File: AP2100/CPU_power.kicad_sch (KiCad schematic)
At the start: 70 parts, among them IC3 AS4C256M16D4-75BCN, IC4 AS4C256M16D4-75BCN, U1 LS1043ASE7KQB

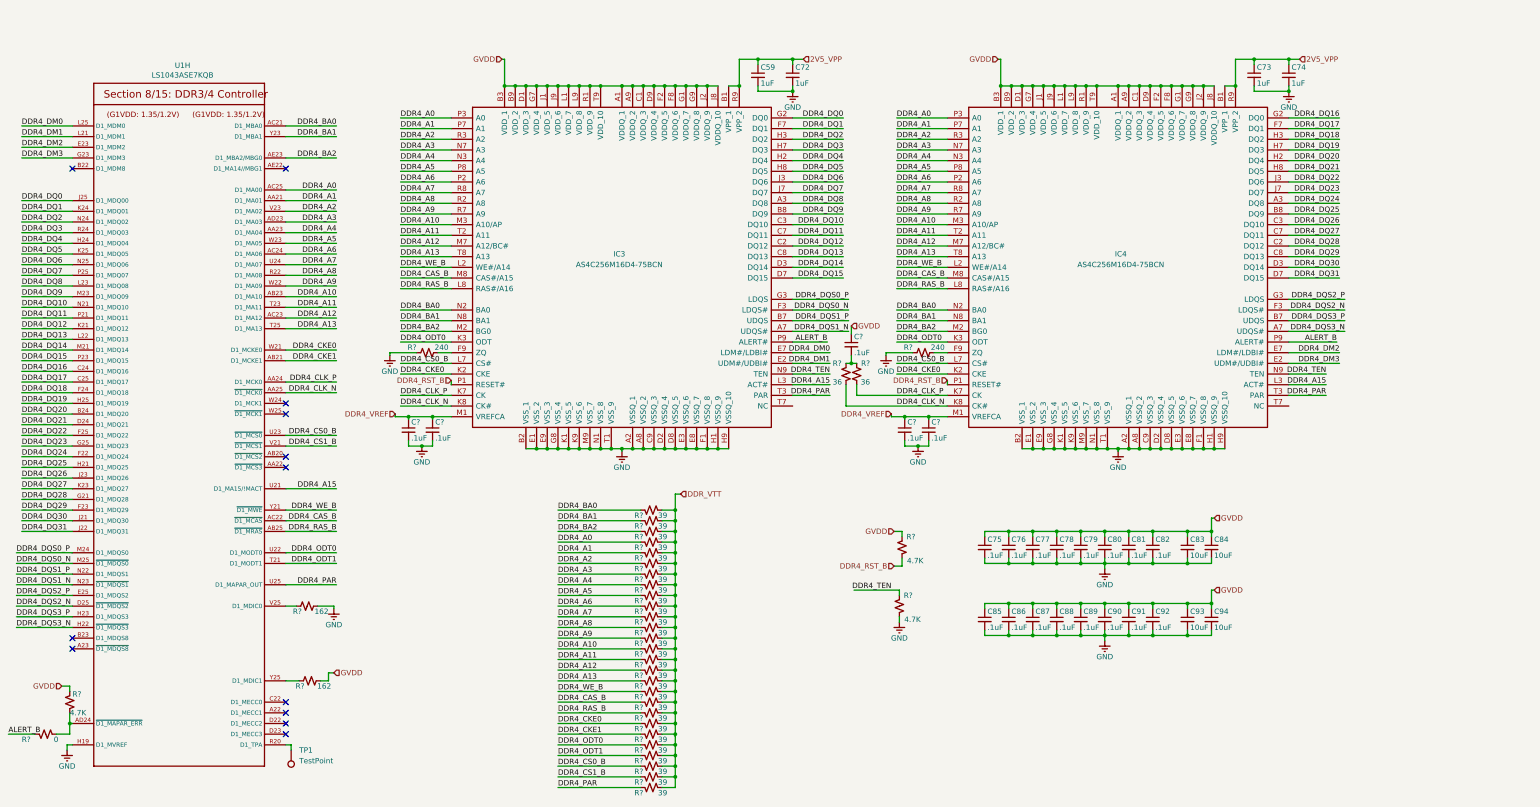
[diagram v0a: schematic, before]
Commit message: Add CPU Power block. Change global labels to hierarchical and link them at top page Add 5V USB power supply
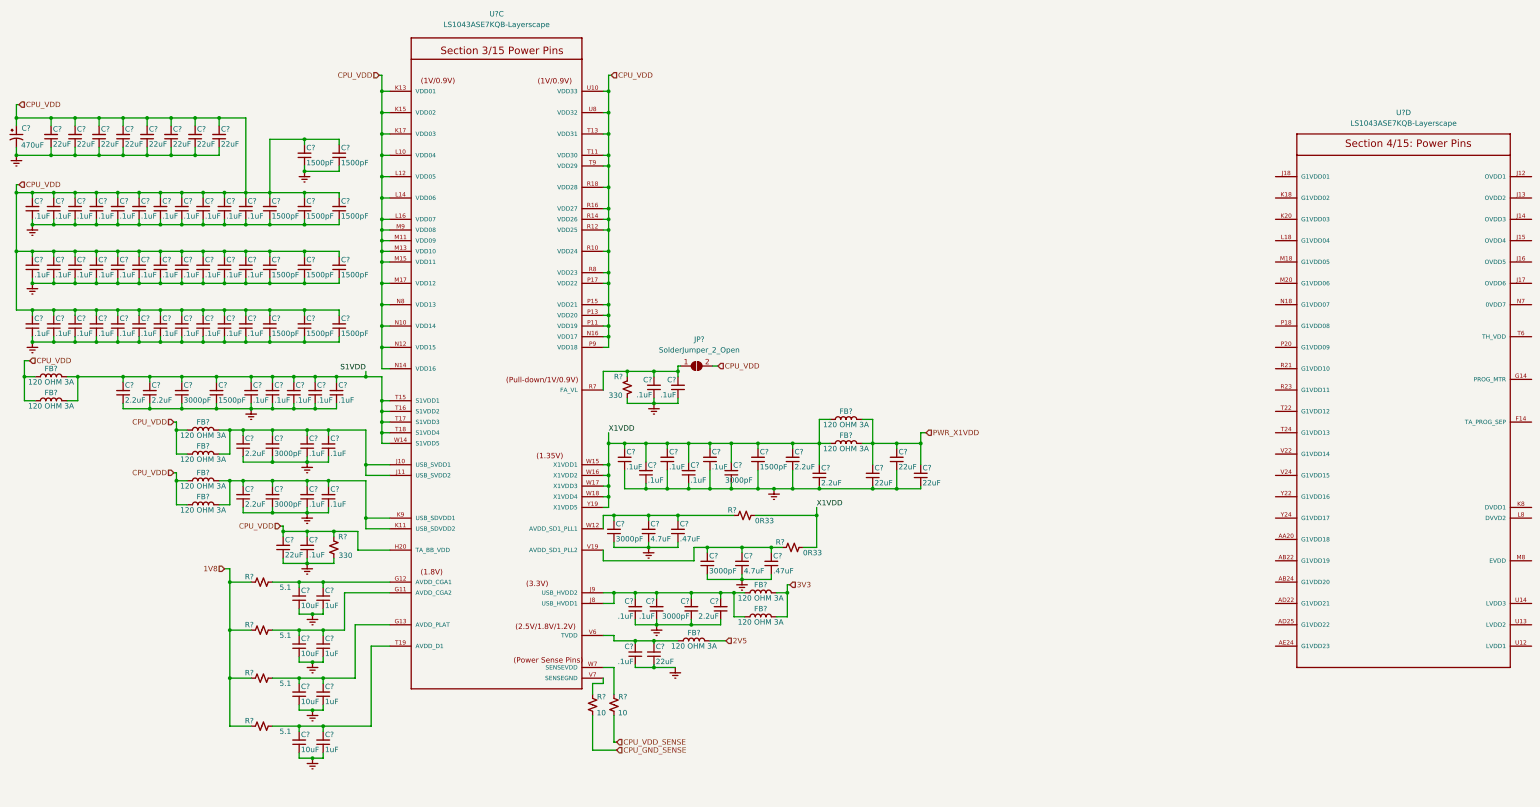
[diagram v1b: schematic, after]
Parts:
- removed C59, C72, C73, C74: 1uF, Capacitor_SMD:C_0402_1005Metric, symbol Device:C_Small
- removed C75, C76, C77, C78, C79, C80, C81, C82, C85, C86, C87, C88, C89, C90, C91, C92, C? (x5): .1uF, Capacitor_SMD:C_0402_1005Metric, symbol Device:C_Small
- removed C83, C84, C93, C94: 10uF, Capacitor_SMD:C_0805_2012Metric, symbol Device:C_Small
- removed IC3, IC4: AS4C256M16D4-75BCN, Scott:BGA96C80P9X16_750X1350X120, symbol Scott:AS4C256M16D4
- removed R? (x27): 39, Resistor_SMD:R_0402_1005Metric, symbol Device:R_Small_US
- removed R? (x2): 36, Resistor_SMD:R_0402_1005Metric, symbol Device:R_Small_US
- removed R? (x2): 240, Resistor_SMD:R_0402_1005Metric, symbol Device:R_Small_US
- removed R? (x3): 4.7K, Resistor_SMD:R_0402_1005Metric, symbol Device:R_Small_US
- removed R?: 0, Resistor_SMD:R_0402_1005Metric, symbol Device:R_Small_US
- removed R? (x2): 162, Resistor_SMD:R_0402_1005Metric, symbol Device:R_Small_US
- removed TP1: TestPoint, symbol Connector:TestPoint
- removed U1: LS1043ASE7KQB, PLS1043ASE7QQA:BGA621C80P25X25_2100X2100X192N, symbol AP2100-rescue:LS1043ASE7KQB-Layerscape
- added C? (x53): .1uF, Capacitor_SMD:C_0201_0603Metric, symbol Device:C_Small
- added C? (x7): 2.2uF, Capacitor_SMD:C_0402_1005Metric, symbol Device:C_Small
- added C? (x13): 22uF, Capacitor_SMD:C_0805_2012Metric, symbol Device:C_Small
- added C? (x2): 4.7uF, Capacitor_SMD:C_0805_2012Metric, symbol Device:C_Small
- added C? (x7): 3000pF, Capacitor_SMD:C_0402_1005Metric, symbol Device:C_Small
- added C? (x12): 1500pF, Capacitor_SMD:C_0201_0603Metric, symbol Device:C_Small
- added C? (x4): 1uF, Capacitor_SMD:C_0201_0603Metric, symbol Device:C_Small
- added C? (x4): 10uF, Capacitor_SMD:C_0805_2012Metric, symbol Device:C_Small
- added C?: 470uF, Capacitor_SMD:C_Elec_10x10.2, symbol Device:CP1_Small
- added C?: 1500pF, Capacitor_SMD:C_0402_1005Metric, symbol Device:C_Small
- added C? (x2): .47uF, Capacitor_SMD:C_0603_1608Metric, symbol Device:C_Small
- added FB? (x11): 120 OHM 3A, Inductor_SMD:L_0603_1608Metric, symbol Device:L
- added JP?: SolderJumper_2_Open, symbol Jumper:SolderJumper_2_Open
- added R? (x2): 10, Resistor_SMD:R_0402_1005Metric, symbol Device:R_Small_US
- added R? (x4): 5.1, Resistor_SMD:R_0402_1005Metric, symbol Device:R_Small_US
- added R? (x2): 330, Resistor_SMD:R_0402_1005Metric, symbol Device:R_Small_US
- added R? (x2): 0R33, Resistor_SMD:R_0402_1005Metric, symbol Device:R_Small_US
- added U? (x2): LS1043ASE7KQB-Layerscape, PLS1043ASE7QQA:BGA621C80P25X25_2100X2100X192N, symbol AP2100-rescue:LS1043ASE7KQB-Layerscape
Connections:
- net GND: now also C?.1, C?.1, C?.1, C?.1, C?.1, C?.1, C?.1, C?.1, C?.1, C?.1, C?.1, C?.1, C?.1, C?.1, C?.1, C?.1, C?.1, C?.1, C?.1, C?.1, C?.1, C?.1, C?.1, C?.1, C?.1, C?.1, C?.1, C?.1, C?.1, C?.1, C?.1, C?.1, C?.1, C?.1, C?.1, C?.1, C?.1, C?.1, C?.1, C?.1, C?.1, C?.1, C?.1, C?.1, C?.1, C?.1, C?.1, C?.1, C?.1, C?.1, C?.1, C?.1, C?.1, C?.1, C?.1, C?.1, C?.1, C?.1, C?.1, C?.1, C?.1, C?.1, C?.1, C?.1, C?.1, C?.1, C?.1, C?.1, C?.1, C?.1, C?.1, C?.1, C?.1, C?.1, C?.1, C?.1, C?.1, C?.1, C?.1, C?.1, C?.1, C?.1, C?.1, C?.1, C?.1, C?.1, C?.1, C?.1, C?.1, C?.1, C?.1, C?.1, C?.1, C?.1, C?.1, C?.1, C?.1, C?.1, C?.1, C?.1, C?.1, C?.1, C?.1, C?.1, C?.1, C?.2, R?.1, R?.1
- new net: C?.2, C?.2, C?.2, R?.1, U?.W12 (AVDD_SD1_PLL1)
- new net: R?.2, U?.W7 (SENSEVDD)
- new net: C?.2, C?.2, R?.2, U?.G11 (AVDD_CGA2)
- new net: C?.2, C?.2, FB?.2, U?.V6 (TVDD)
- new net: C?.2, C?.2, R?.2, U?.G12 (AVDD_CGA1)
- new net: C?.2, C?.2, C?.2, C?.2, FB?.2, FB?.2, U?.K11 (USB_SDVDD2), U?.K9 (USB_SDVDD1)
- new net: C?.2, C?.2, C?.2, C?.2, FB?.2, FB?.2, U?.J8 (USB_HVDD1), U?.J9 (USB_HVDD2)
- new net: C?.2, C?.2, R?.2, U?.T19 (AVDD_D1)
- new net: C?.2, C?.2, C?.2, C?.2, FB?.2, FB?.2, U?.J10 (USB_SVDD1), U?.J11 (USB_SVDD2)
- new net: C?.2, C?.2, JP?.1 (A), R?.2, U?.R7 (FA_VL)
- new net: C?.2, C?.2, C?.2, R?.1, U?.V19 (AVDD_SD1_PLL2)
- new net: C?.2, C?.2, R?.2, U?.G13 (AVDD_PLAT)
- new net: R?.2, U?.V7 (SENSEGND)
- new net 1V8: R?.1, R?.1, R?.1, R?.1
- new net 2V5: FB?.1
- new net 3V3: FB?.1, FB?.1
- new net CPU_GND_SENSE: R?.1
- new net CPU_VDD: C?.1, C?.2, C?.2, C?.2, C?.2, C?.2, C?.2, C?.2, C?.2, C?.2, C?.2, C?.2, C?.2, C?.2, C?.2, C?.2, C?.2, C?.2, C?.2, C?.2, C?.2, C?.2, C?.2, C?.2, C?.2, C?.2, C?.2, C?.2, C?.2, C?.2, C?.2, C?.2, C?.2, C?.2, C?.2, C?.2, C?.2, C?.2, C?.2, C?.2, C?.2, C?.2, C?.2, C?.2, C?.2, C?.2, C?.2, C?.2, C?.2, C?.2, C?.2, C?.2, C?.2, C?.2, C?.2, FB?.1, FB?.1, FB?.1, FB?.1, FB?.1, FB?.1, JP?.2 (B), R?.2, U?.H20 (TA_BB_VDD), U?.K13 (VDD01), U?.K15 (VDD02), U?.K17 (VDD03), U?.L10 (VDD04), U?.L12 (VDD05), U?.L14 (VDD06), U?.L16 (VDD07), U?.M11 (VDD09), U?.M13 (VDD10), U?.M15 (VDD11), U?.M17 (VDD12), U?.M9 (VDD08), U?.N10 (VDD14), U?.N12 (VDD15), U?.N14 (VDD16), U?.N16 (VDD17), U?.N8 (VDD13), U?.P11 (VDD19), U?.P13 (VDD20), U?.P15 (VDD21), U?.P17 (VDD22), U?.P9 (VDD18), U?.R10 (VDD24), U?.R12 (VDD25), U?.R14 (VDD26), U?.R16 (VDD27), U?.R18 (VDD28), U?.R8 (VDD23), U?.T11 (VDD30), U?.T13 (VDD31), U?.T9 (VDD29), U?.U10 (VDD33), U?.U8 (VDD32)
- new net CPU_VDD_SENSE: R?.1
- new net PWR_X1VDD: C?.2, C?.2, C?.2, FB?.2, FB?.2
- new net S1VDD: C?.2, C?.2, C?.2, C?.2, C?.2, C?.2, C?.2, C?.2, C?.2, FB?.2, FB?.2, U?.T15 (S1VDD1), U?.T16 (S1VDD2), U?.T17 (S1VDD3), U?.T18 (S1VDD4), U?.W14 (S1VDD5)
- new net X1VDD: C?.2, C?.2, C?.2, C?.2, C?.2, C?.2, C?.2, C?.2, C?.2, FB?.1, FB?.1, R?.2, R?.2, U?.W15 (X1VDD1), U?.W16 (X1VDD2), U?.W17 (X1VDD3), U?.W18 (X1VDD4), U?.Y19 (X1VDD5)
- no-connect marks 12 -> 0
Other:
- company: IS ImageStream Internet Solutions, Inc. -> (none)
- title: AP2100 -> (none)

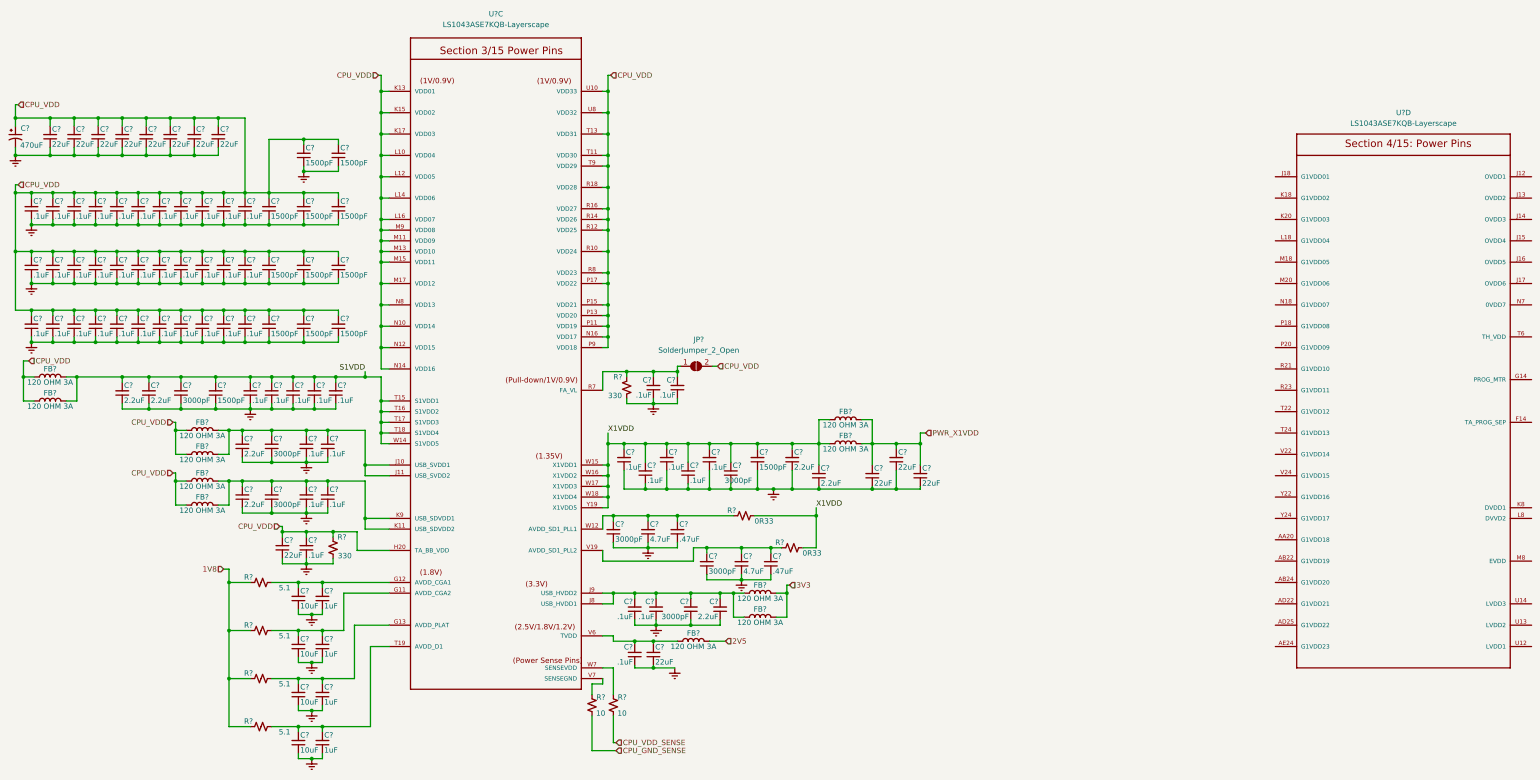
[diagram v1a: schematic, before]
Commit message: Add 2nd CPU power page. Start reset block
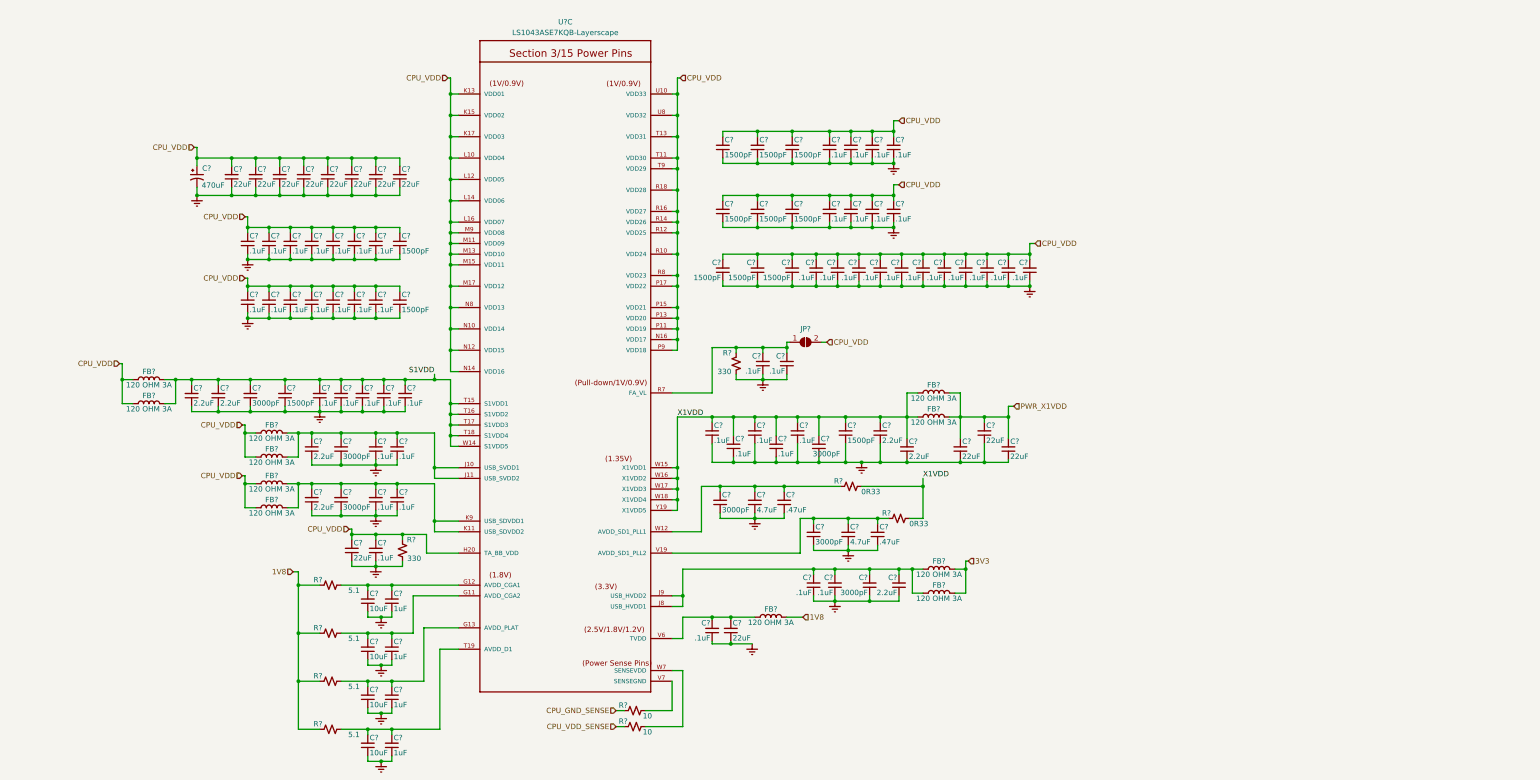
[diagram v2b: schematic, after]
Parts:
- removed R?: 10, Resistor_SMD:R_0402_1005Metric, symbol Device:R_Small_US
- removed U?: LS1043ASE7KQB-Layerscape, PLS1043ASE7QQA:BGA621C80P25X25_2100X2100X192N, symbol AP2100-rescue:LS1043ASE7KQB-Layerscape
- added R?: 10, Resistor_SMD:R_0402_1005Metric, symbol Device:R_Small_US
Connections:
- net 2V5 is gone; now on net 1V8: FB?.1
- net CPU_GND_SENSE: now also R?.2; no longer R?.1
- net CPU_VDD_SENSE: now also R?.2
- net at U?.W7 (SENSEVDD): now also R?.1
- net at U?.V7 (SENSEGND): now also R?.1; no longer R?.2
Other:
- moved on the sheet: C?, FB?, JP?, R?, U?C

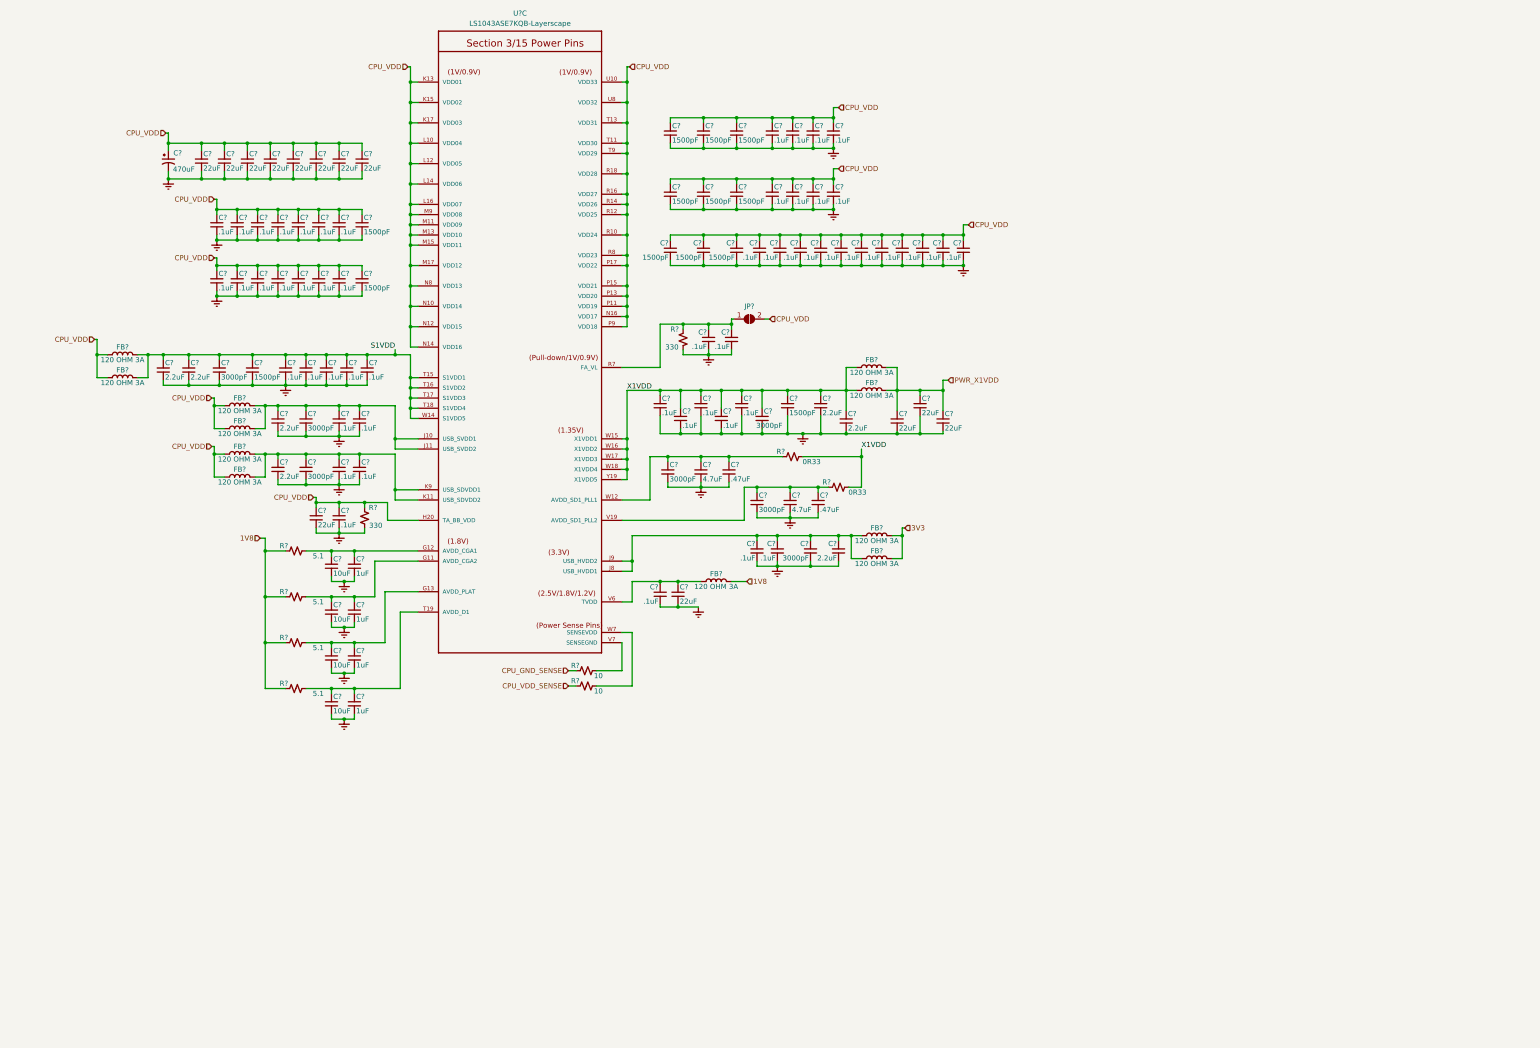
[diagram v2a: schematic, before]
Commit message: Add clocking and start of ethernet
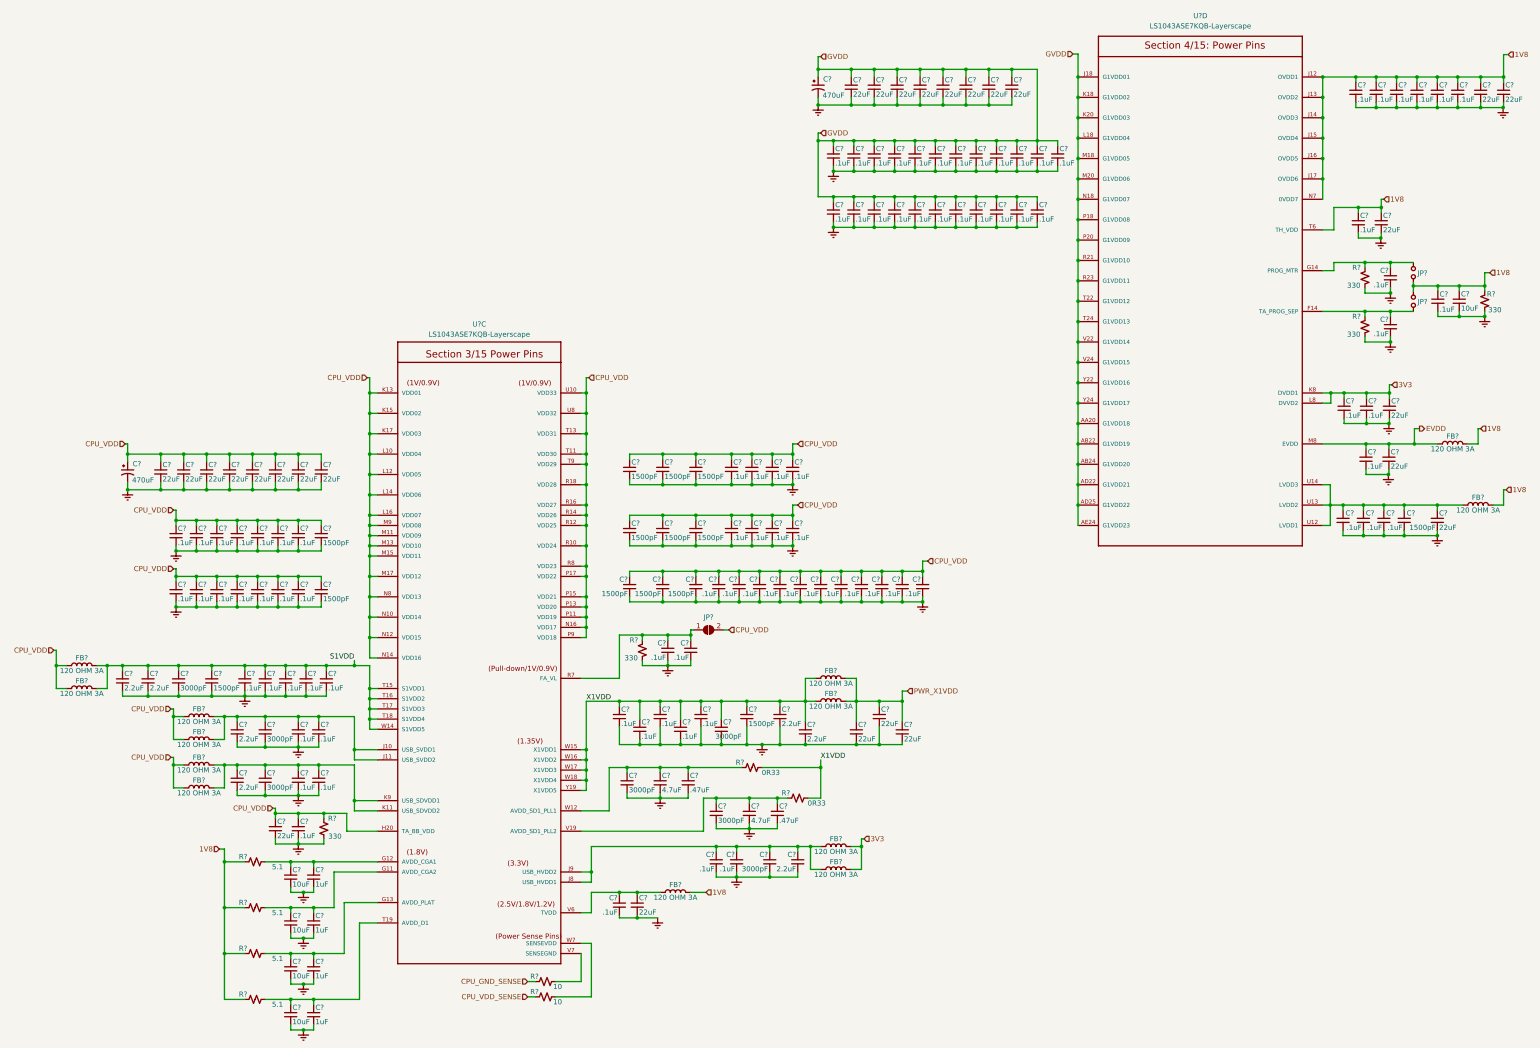
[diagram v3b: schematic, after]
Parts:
- added C? (x39): .1uF, Capacitor_SMD:C_0201_0603Metric, symbol Device:C_Small
- added C? (x14): 22uF, Capacitor_SMD:C_0805_2012Metric, symbol Device:C_Small
- added C?: 10uF, Capacitor_SMD:C_0805_2012Metric, symbol Device:C_Small
- added C?: 1500pF, Capacitor_SMD:C_0201_0603Metric, symbol Device:C_Small
- added C?: 470uF, Capacitor_SMD:C_Elec_10x10.2, symbol Device:CP1_Small
- added FB? (x2): 120 OHM 3A, Inductor_SMD:L_0603_1608Metric, symbol Device:L
- added JP? (x2): SolderJumper_2_Open, symbol Device:Jumper_NO_Small
- added R? (x3): 330, Resistor_SMD:R_0402_1005Metric, symbol Device:R_Small_US
- added U?: LS1043ASE7KQB-Layerscape, PLS1043ASE7QQA:BGA621C80P25X25_2100X2100X192N, symbol AP2100-rescue:LS1043ASE7KQB-Layerscape
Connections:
- net 1V8: now also C?.1, C?.2, C?.2, C?.2, C?.2, C?.2, C?.2, C?.2, C?.2, C?.2, C?.2, C?.2, FB?.1, FB?.1, JP?.1, JP?.2, R?.1, U?.J12 (OVDD1), U?.J13 (OVDD2), U?.J14 (OVDD3), U?.J15 (OVDD4), U?.J16 (OVDD5), U?.J17 (OVDD6), U?.N7 (0VDD7), U?.T6 (TH_VDD)
- net 3V3: now also C?.2, C?.2, C?.2, U?.K8 (DVDD1), U?.L8 (DVVD2)
- net GND: now also C?.1, C?.1, C?.1, C?.1, C?.1, C?.1, C?.1, C?.1, C?.1, C?.1, C?.1, C?.1, C?.1, C?.1, C?.1, C?.1, C?.1, C?.1, C?.1, C?.1, C?.1, C?.1, C?.1, C?.1, C?.1, C?.1, C?.1, C?.1, C?.1, C?.1, C?.1, C?.1, C?.1, C?.1, C?.1, C?.1, C?.1, C?.1, C?.1, C?.1, C?.1, C?.1, C?.1, C?.1, C?.1, C?.1, C?.1, C?.1, C?.1, C?.1, C?.1, C?.1, C?.1, C?.1, C?.2, C?.2, R?.1, R?.1, R?.2
- new net: C?.2, C?.2, C?.2, C?.2, C?.2, FB?.2, U?.U12 (LVDD1), U?.U13 (LVDD2), U?.U14 (LVDD3)
- new net: C?.2, JP?.2, R?.2, U?.G14 (PROG_MTR)
- new net: C?.2, JP?.1, R?.2, U?.F14 (TA_PROG_SEP)
- new net EVDD: C?.2, C?.2, FB?.2, U?.M8 (EVDD)
- new net GVDD: C?.1, C?.2, C?.2, C?.2, C?.2, C?.2, C?.2, C?.2, C?.2, C?.2, C?.2, C?.2, C?.2, C?.2, C?.2, C?.2, C?.2, C?.2, C?.2, C?.2, C?.2, C?.2, C?.2, C?.2, C?.2, C?.2, C?.2, C?.2, C?.2, C?.2, C?.2, C?.2, U?.AA20 (G1VDD18), U?.AB22 (G1VDD19), U?.AB24 (G1VDD20), U?.AD22 (G1VDD21), U?.AD25 (G1VDD22), U?.AE24 (G1VDD23), U?.J18 (G1VDD01), U?.K18 (G1VDD02), U?.K20 (G1VDD03), U?.L18 (G1VDD04), U?.M18 (G1VDD05), U?.M20 (G1VDD06), U?.N18 (G1VDD07), U?.P18 (G1VDD08), U?.P20 (G1VDD09), U?.R21 (G1VDD10), U?.R23 (G1VDD11), U?.T22 (G1VDD12), U?.T24 (G1VDD13), U?.V22 (G1VDD14), U?.V24 (G1VDD15), U?.Y22 (G1VDD16), U?.Y24 (G1VDD17)
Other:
- moved on the sheet: C?, FB?, JP?, R?, U?C
